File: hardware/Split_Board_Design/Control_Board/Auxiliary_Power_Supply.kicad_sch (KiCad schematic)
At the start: 25 parts, among them U7 TLV1117-33, U8 LV14340DDAR

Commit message: feat(layout): Finished demo schematic for control board
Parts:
- C1: value 100uF -> 680uF-35V; footprint Capacitor_SMD:CP_Elec_8x10.5 -> RobotChargeController:CP_Elec_12.5x13.5_Generic_H13
- C20, C42: footprint Capacitor_SMD:C_0805_2012Metric -> Capacitor_SMD:C_0603_1608Metric; Link to Buy https://linhkien.cxtvn.com/1976-tu-khong-phan-cuc-0805.html -> https://linhkien.cxtvn.com/1982-tu-105-1uf-0603-50v-10-20c.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
- C27, C28: footprint Capacitor_SMD:C_0805_2012Metric -> Capacitor_SMD:C_0603_1608Metric; Link to Buy https://linhkien.cxtvn.com/1976-tu-khong-phan-cuc-0805.html -> https://linhkien.cxtvn.com/2886-tu-106-10uf-0603-50v-10-20c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
- U8: Link to Buy (none) -> https://banlinhkiendientu.vn/lv14340ddar-14340-ic-nguon-sop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

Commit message: feat(layout): Update layout
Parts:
- C1: Link to Buy https://linhkien.cxtvn.com/3033-tu-nhom-100uf-50v-8x105-5c.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 -> https://linhkien.cxtvn.com/3037-tu-nhom-680uf-35v-125x135mm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
- C13: value 33pF -> 33pF-50V; footprint Capacitor_SMD:C_0805_2012Metric -> Capacitor_SMD:C_0603_1608Metric; Link to Buy https://linhkien.cxtvn.com/1976-tu-khong-phan-cuc-0805.html -> https://linhkien.cxtvn.com/3426-tu-330-33pf-0603-50v-20c.ht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
- C16, C17: value 22uF -> 22uF-50V
- C18: value 100nF -> 100nF-50V; footprint Capacitor_SMD:C_0805_2012Metric -> Capacitor_SMD:C_0603_1608Metric; Link to Buy https://linhkien.cxtvn.com/1976-tu-khong-phan-cuc-0805.html -> https://linhkien.cxtvn.com/1981-tu-0603-khong-phan-cuc.html
- C6: value 22nF -> 22nF-50V
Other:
- moved on the sheet: C1, C27
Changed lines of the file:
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@@
 	)
 	(junction
-		(at 214.63 66.04)
+		(at 54.61 58.42)
 		(diameter 0)
 		(color 0 0 0 0)
 	)
 	(junction
-		(at 157.48 76.2)
+		(at 214.63 66.04)
 		(diameter 0)
 		(color 0 0 0 0)
 	)
 	(junction
-		(at 109.22 58.42)
+		(at 157.48 76.2)
 		(diameter 0)
 		(color 0 0 0 0)
 	)
 	(junction
-		(at 224.79 41.91)
+		(at 109.22 58.42)
 		(diameter 0)
 		(color 0 0 0 0)
 	)
 	(junction
-		(at 96.52 58.42)
+		(at 224.79 41.91)
 		(diameter 0)
 		(color 0 0 0 0)
@@
 	)
 	(junction
+		(at 96.52 58.42)
+		(diameter 0)
+		(color 0 0 0 0)
+	)
+	(junction
 		(at 134.62 114.3)
 		(diameter 0)
@@
 	)
 	(junction
+		(at 62.23 58.42)
+		(diameter 0)
+		(color 0 0 0 0)
+	)
+	(junction
 		(at 190.5 41.91)
 		(diameter 0)
@@
 	)
 	(junction
-		(at 67.31 58.42)
-		(diameter 0)
-		(color 0 0 0 0)
-	)
-	(junction
-		(at 82.55 58.42)
+		(at 76.2 58.42)
 		(diameter 0)
 		(color 0 0 0 0)
@@
 		(color 0 0 0 0)
 	)
-	(junction
-		(at 54.61 58.42)
-		(diameter 0)
-		(color 0 0 0 0)
-	)
 	(no_connect
 		(at 133.35 60.96)
@@
 	(wire
 		(pts
-			(xy 67.31 58.42) (xy 67.31 64.77)
+			(xy 62.23 58.42) (xy 62.23 64.77)
 		)
 		(stroke
@@
 	(wire
 		(pts
-			(xy 67.31 58.42) (xy 82.55 58.42)
+			(xy 62.23 58.42) (xy 76.2 58.42)
 		)
 		(stroke
@@
 	(wire
 		(pts
-			(xy 82.55 71.12) (xy 82.55 78.74)
+			(xy 76.2 71.12) (xy 76.2 78.74)
 		)
 		(stroke
@@
 	(wire
 		(pts
-			(xy 54.61 58.42) (xy 67.31 58.42)
+			(xy 54.61 58.42) (xy 62.23 58.42)
 		)
 		(stroke
@@
 	(wire
 		(pts
-			(xy 82.55 55.88) (xy 82.55 58.42)
+			(xy 76.2 55.88) (xy 76.2 58.42)
 		)
 		(stroke
@@
 	(wire
 		(pts
-			(xy 82.55 58.42) (xy 82.55 66.04)
+			(xy 76.2 58.42) (xy 76.2 66.04)
 		)
 		(stroke
@@
 	(wire
 		(pts
-			(xy 67.31 78.74) (xy 67.31 72.39)
+			(xy 62.23 78.74) (xy 62.23 72.39)
 		)
 		(stroke
@@
 	(wire
 		(pts
-			(xy 82.55 58.42) (xy 96.52 58.42)
+			(xy 76.2 58.42) (xy 96.52 58.42)
 		)
 		(stroke
@@
 	(symbol
 		(lib_id "power:GND")
-		(at 82.55 78.74 0)
+		(at 76.2 78.74 0)
 		(unit 1)
 		(body_style 1)
@@
 		(fields_autoplaced yes)
 		(property "Reference" "#PWR072"
-			(at 82.55 85.09 0)
+			(at 76.2 85.09 0)
 			(hide yes)
 			(show_name no)
@@
 		)
 		(property "Value" "GND"
-			(at 82.55 83.82 0)
+			(at 76.2 83.82 0)
 			(show_name no)
 			(do_not_autoplace no)
@@
 		)
 		(property "Footprint" ""
-			(at 82.55 78.74 0)
+			(at 76.2 78.74 0)
 			(hide yes)
 			(show_name no)
@@
 		)
 		(property "Datasheet" ""
-			(at 82.55 78.74 0)
+			(at 76.2 78.74 0)
 			(hide yes)
 			(show_name no)
@@
 		)
 		(property "Description" "Power symbol creates a global label with name \"GND\" , ground"
-			(at 82.55 78.74 0)
+			(at 76.2 78.74 0)
 			(hide yes)
 			(show_name no)
@@
 			)
 		)
-		(property "Value" "22uF"
+		(property "Value" "22uF-50V"
 			(at 238.76 60.9662 0)
 			(show_name no)
@@
 			)
 		)
-		(property "Value" "22uF"
+		(property "Value" "22uF-50V"
 			(at 227.33 60.9662 0)
 			(show_name no)
@@
 	(symbol
 		(lib_id "power:GND")
-		(at 67.31 78.74 0)
+		(at 62.23 78.74 0)
 		(unit 1)
 		(body_style 1)
@@
 		(dnp no)
 		(property "Reference" "#PWR086"
-			(at 67.31 85.09 0)
+			(at 62.23 85.09 0)
 			(hide yes)
 			(show_name no)
@@
 		)
 		(property "Value" "GND"
-			(at 67.31 82.55 0)
+			(at 62.23 82.55 0)
 			(show_name no)
 			(do_not_autoplace no)
@@
 		)
 		(property "Footprint" ""
-			(at 67.31 78.74 0)
+			(at 62.23 78.74 0)
 			(hide yes)
 			(show_name no)
@@
 		)
 		(property "Datasheet" ""
-			(at 67.31 78.74 0)
+			(at 62.23 78.74 0)
 			(hide yes)
 			(show_name no)
@@
 		)
 		(property "Description" "Power symbol creates a global label with name \"GND\" , ground"
-			(at 67.31 78.74 0)
+			(at 62.23 78.74 0)
 			(hide yes)
 			(show_name no)
@@
 			)
 		)
-		(property "Value" "100nF"
+		(property "Value" "100nF-50V"
 			(at 250.19 60.9662 0)
 			(show_name no)
@@
 			)
 		)
-		(property "Footprint" "Capacitor_SMD:C_0805_2012Metric"
+		(property "Footprint" "Capacitor_SMD:C_0603_1608Metric"
 			(at 247.65 59.69 0)
 			(hide yes)
@@
 			)
 		)
-		(property "Link to Buy" "https://linhkien.cxtvn.com/1976-tu-khong-phan-cuc-0805.html"
+		(property "Link to Buy" "https://linhkien.cxtvn.com/1981-tu-0603-khong-phan-cuc.html"
 			(at 10.16 0 0)
 			(hide yes)
@@
 	(symbol
 		(lib_id "power:PWR_FLAG")
-		(at 82.55 55.88 0)
+		(at 76.2 55.88 0)
 		(unit 1)
 		(body_style 1)
@@
 		(fields_autoplaced yes)
 		(property "Reference" "#FLG010"
-			(at 82.55 53.975 0)
+			(at 76.2 53.975 0)
 			(hide yes)
 			(show_name no)
@@
 		)
 		(property "Value" "PWR_FLAG"
-			(at 82.55 50.8 0)
+			(at 76.2 50.8 0)
 			(show_name no)
 			(do_not_autoplace no)
@@
 		)
 		(property "Footprint" ""
-			(at 82.55 55.88 0)
+			(at 76.2 55.88 0)
 			(hide yes)
 			(show_name no)
@@
 		)
 		(property "Datasheet" ""
-			(at 82.55 55.88 0)
+			(at 76.2 55.88 0)
 			(hide yes)
 			(show_name no)
@@
 		)
 		(property "Description" "Special symbol for telling ERC where power comes from"
-			(at 82.55 55.88 0)
+			(at 76.2 55.88 0)
 			(hide yes)
 			(show_name no)
@@
 	(symbol
 		(lib_id "Device:C_Polarized")
-		(at 67.31 68.58 0)
+		(at 62.23 68.58 0)
 		(unit 1)
 		(body_style 1)
@@
 		(dnp no)
 		(property "Reference" "C1"
-			(at 68.072 71.374 0)
+			(at 62.992 71.374 0)
 			(show_name no)
 			(do_not_autoplace no)
@@
 		)
 		(property "Value" "680uF-35V"
-			(at 68.072 73.914 0)
+			(at 62.992 73.914 0)
 			(show_name no)
 			(do_not_autoplace no)
@@
 		)
 		(property "Footprint" "RobotChargeController:CP_Elec_12.5x13.5_Generic_H13"
-			(at 68.2752 72.39 0)
+			(at 63.1952 72.39 0)
 			(hide yes)
 			(show_name no)
@@
 		)
 		(property "Datasheet" ""
-			(at 67.31 68.58 0)
+			(at 62.23 68.58 0)
 			(hide yes)
 			(show_name no)
@@
 		)
 		(property "Description" "Polarized capacitor"
-			(at 67.31 68.58 0)
+			(at 62.23 68.58 0)
 			(hide yes)
 			(show_name no)
@@
 			)
 		)
-		(property "Link to Buy" "https://linhkien.cxtvn.com/3033-tu-nhom-100uf-50v-8x105-5c.html"
-			(at 67.31 68.58 0)
+		(property "Link to Buy" "https://linhkien.cxtvn.com/3037-tu-nhom-680uf-35v-125x135mm.html"
+			(at 62.23 68.58 0)
 			(hide yes)
 			(show_name no)
@@
 		)
 		(property "CREATOR" ""
-			(at 67.31 68.58 0)
+			(at 62.23 68.58 0)
 			(hide yes)
 			(show_name no)
@@
 			)
 		)
-		(property "Value" "22nF"
+		(property "Value" "22nF-50V"
 			(at 191.77 72.3962 0)
 			(show_name no)
@@
 			)
 		)
-		(property "Value" "33pF"
+		(property "Value" "33pF-50V"
 			(at 207.01 50.8062 0)
 			(show_name no)
@@
 			)
 		)
-		(property "Footprint" "Capacitor_SMD:C_0805_2012Metric"
+		(property "Footprint" "Capacitor_SMD:C_0603_1608Metric"
 			(at 204.47 49.53 0)
 			(hide yes)
@@
 			)
 		)
-		(property "Link to Buy" "https://linhkien.cxtvn.com/1976-tu-khong-phan-cuc-0805.html"
+		(property "Link to Buy" "https://linhkien.cxtvn.com/3426-tu-330-33pf-0603-50v-20c.html"
 			(at 398.78 0 0)
 			(hide yes)
@@
 	(symbol
 		(lib_id "Device:C_Small")
-		(at 82.55 68.58 0)
+		(at 76.2 68.58 0)
 		(unit 1)
 		(body_style 1)
@@
 		(dnp no)
 		(property "Reference" "C27"
-			(at 82.804 71.1262 0)
+			(at 76.454 71.1262 0)
 			(show_name no)
 			(do_not_autoplace no)
@@
 		)
 		(property "Value" "10uF-50V"
-			(at 83.058 72.898 0)
+			(at 76.708 72.898 0)
 			(show_name no)
 			(do_not_autoplace no)
@@
 		)
 		(property "Footprint" "Capacitor_SMD:C_0603_1608Metric"
-			(at 82.55 68.58 0)
+			(at 76.2 68.58 0)
 			(hide yes)
 			(show_name no)
@@
 		)
 		(property "Datasheet" ""
-			(at 82.55 68.58 0)
+			(at 76.2 68.58 0)
 			(hide yes)
 			(show_name no)
@@
 		)
 		(property "Description" "Unpolarized capacitor, small symbol"
-			(at 82.55 68.58 0)
+			(at 76.2 68.58 0)
 			(hide yes)
 			(show_name no)
@@
 		)
 		(property "Link to Buy" "https://linhkien.cxtvn.com/2886-tu-106-10uf-0603-50v-10-20c.html"
-			(at 5.08 0 0)
+			(at -1.27 0 0)
 			(hide yes)
 			(show_name no)
@@
 		)
 		(property "BOM Comments" ""
-			(at 82.55 68.58 0)
+			(at 76.2 68.58 0)
 			(hide yes)
 			(show_name no)
@@
 		)
 		(property "DigiKey_Part_Number" ""
-			(at 82.55 68.58 0)
+			(at 76.2 68.58 0)
 			(hide yes)
 			(show_name no)
@@
 		)
 		(property "Link" ""
-			(at 82.55 68.58 0)
+			(at 76.2 68.58 0)
 			(hide yes)
 			(show_name no)
@@
 		)
 		(property "Sim.Type" ""
-			(at 82.55 68.58 0)
+			(at 76.2 68.58 0)
 			(hide yes)
 			(show_name no)
@@
 		)
 		(property "VENDOR" ""
-			(at 82.55 68.58 0)
+			(at 76.2 68.58 0)
 			(hide yes)
 			(show_name no)
@@
 		)
 		(property "CREATOR" ""
-			(at 82.55 68.58 0)
+			(at 76.2 68.58 0)
 			(hide yes)
 			(show_name no)

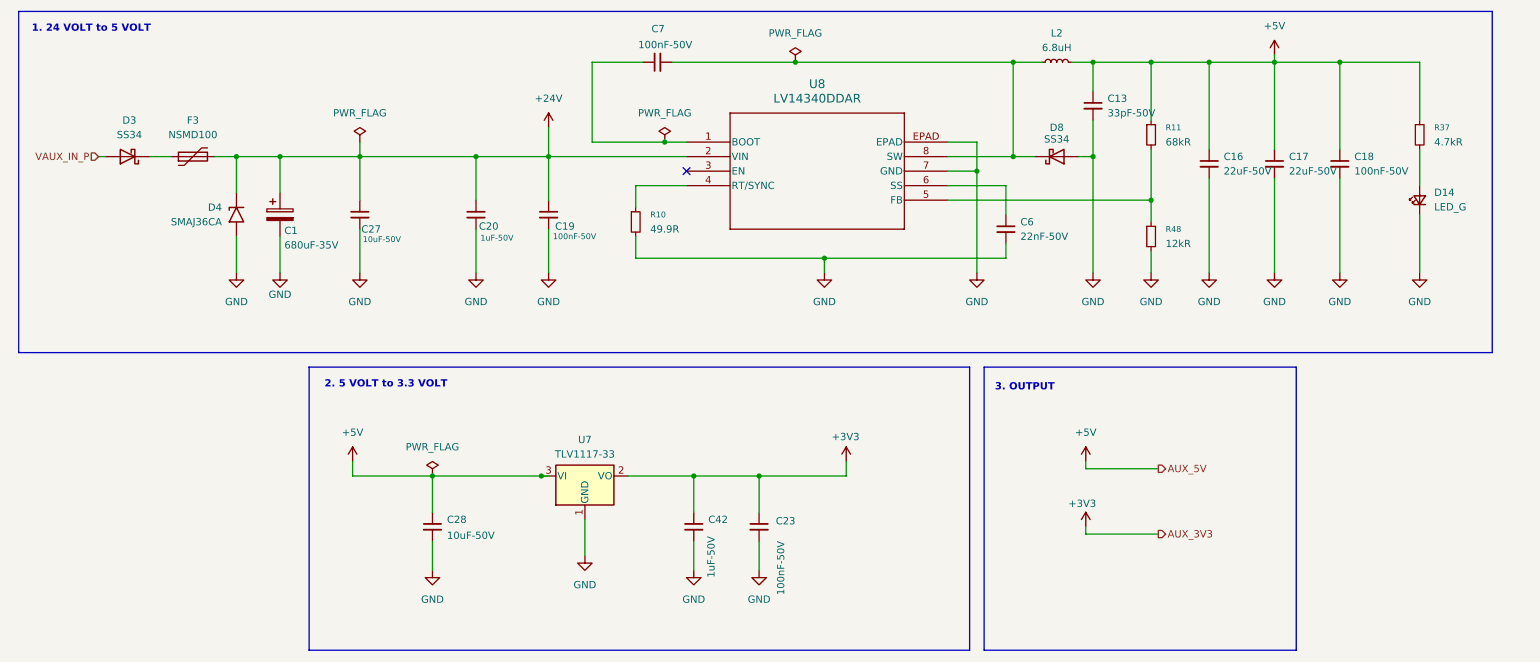
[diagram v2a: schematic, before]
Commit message: feat(schematic): update INA240A2PW to ÍNA240A2D
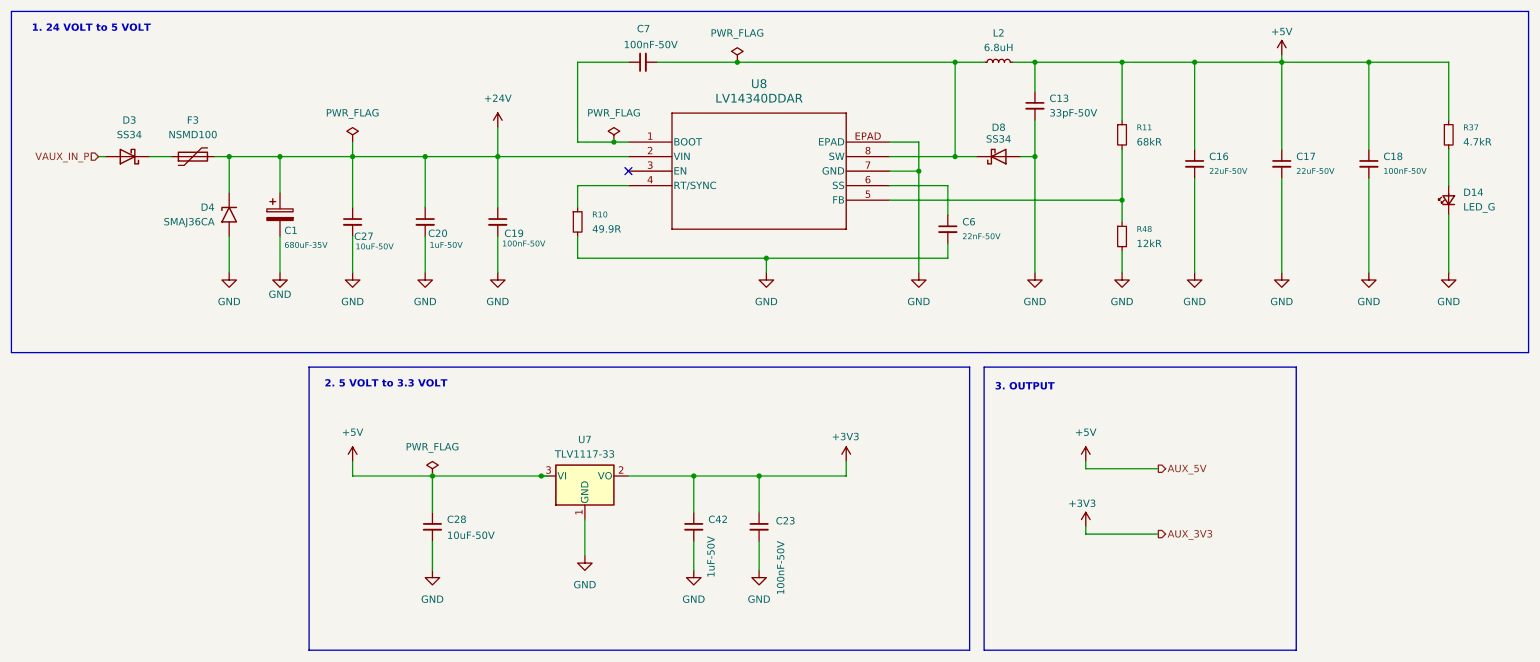
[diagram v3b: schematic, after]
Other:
- moved on the sheet: C13, C16, C17, C18, C19, C20, C27, C6, C7, D14, D4, D8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
